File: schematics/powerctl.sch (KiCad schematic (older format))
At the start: 4 parts

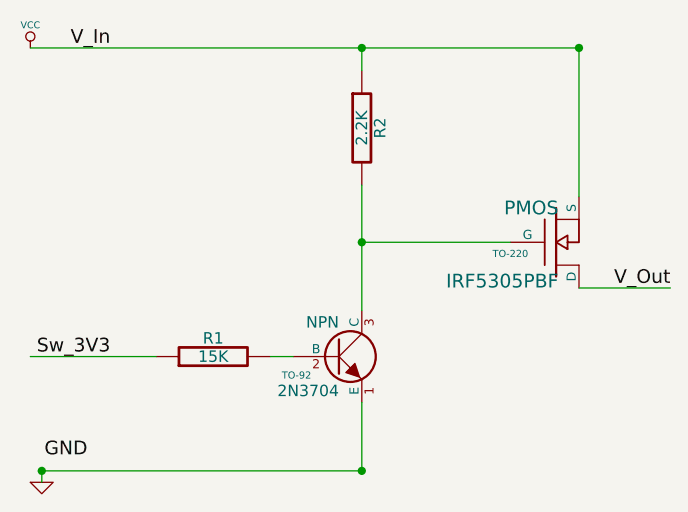
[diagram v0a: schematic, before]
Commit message: Update schematic to use new resistor values Complete "Building design" part of tutorial
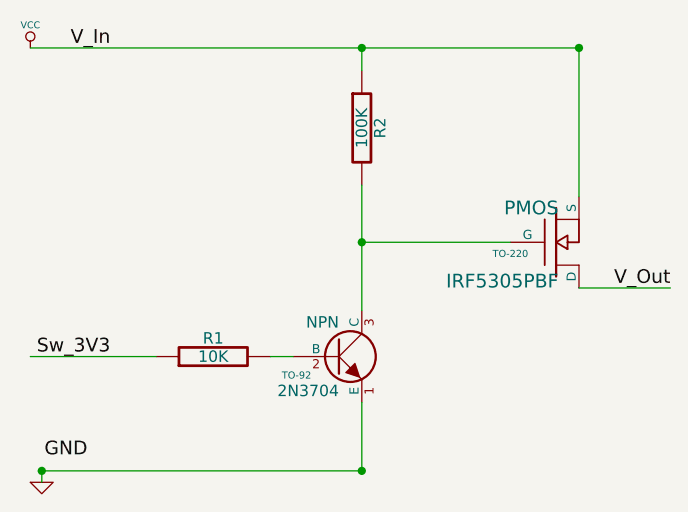
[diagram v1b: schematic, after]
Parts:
- R1: value 15K -> 10K
- R2: value 2.2K -> 100K
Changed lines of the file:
@@
-EESchema Schematic File Version 2  date Mon 19 Aug 2013 14:35:30 BST
+EESchema Schematic File Version 2  date Mon 19 Aug 2013 17:30:26 BST
 LIBS:power
 LIBS:device
@@
 P 1600 2350
 F 0 "R1" V 1680 2350 50  0000 C CNN
-F 1 "15K" V 1600 2350 50  0000 C CNN
+F 1 "10K" V 1600 2350 50  0000 C CNN
 	1    1600 2350
 	0    -1   -1   0
@@
 P 2250 1350
 F 0 "R2" V 2330 1350 50  0000 C CNN
-F 1 "2.2K" V 2250 1350 50  0000 C CNN
+F 1 "100K" V 2250 1350 50  0000 C CNN
 	1    2250 1350
 	1    0    0    -1
